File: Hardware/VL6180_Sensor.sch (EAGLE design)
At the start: 23 parts, among them U1 VL6180, U3 MIC5219 3.3V

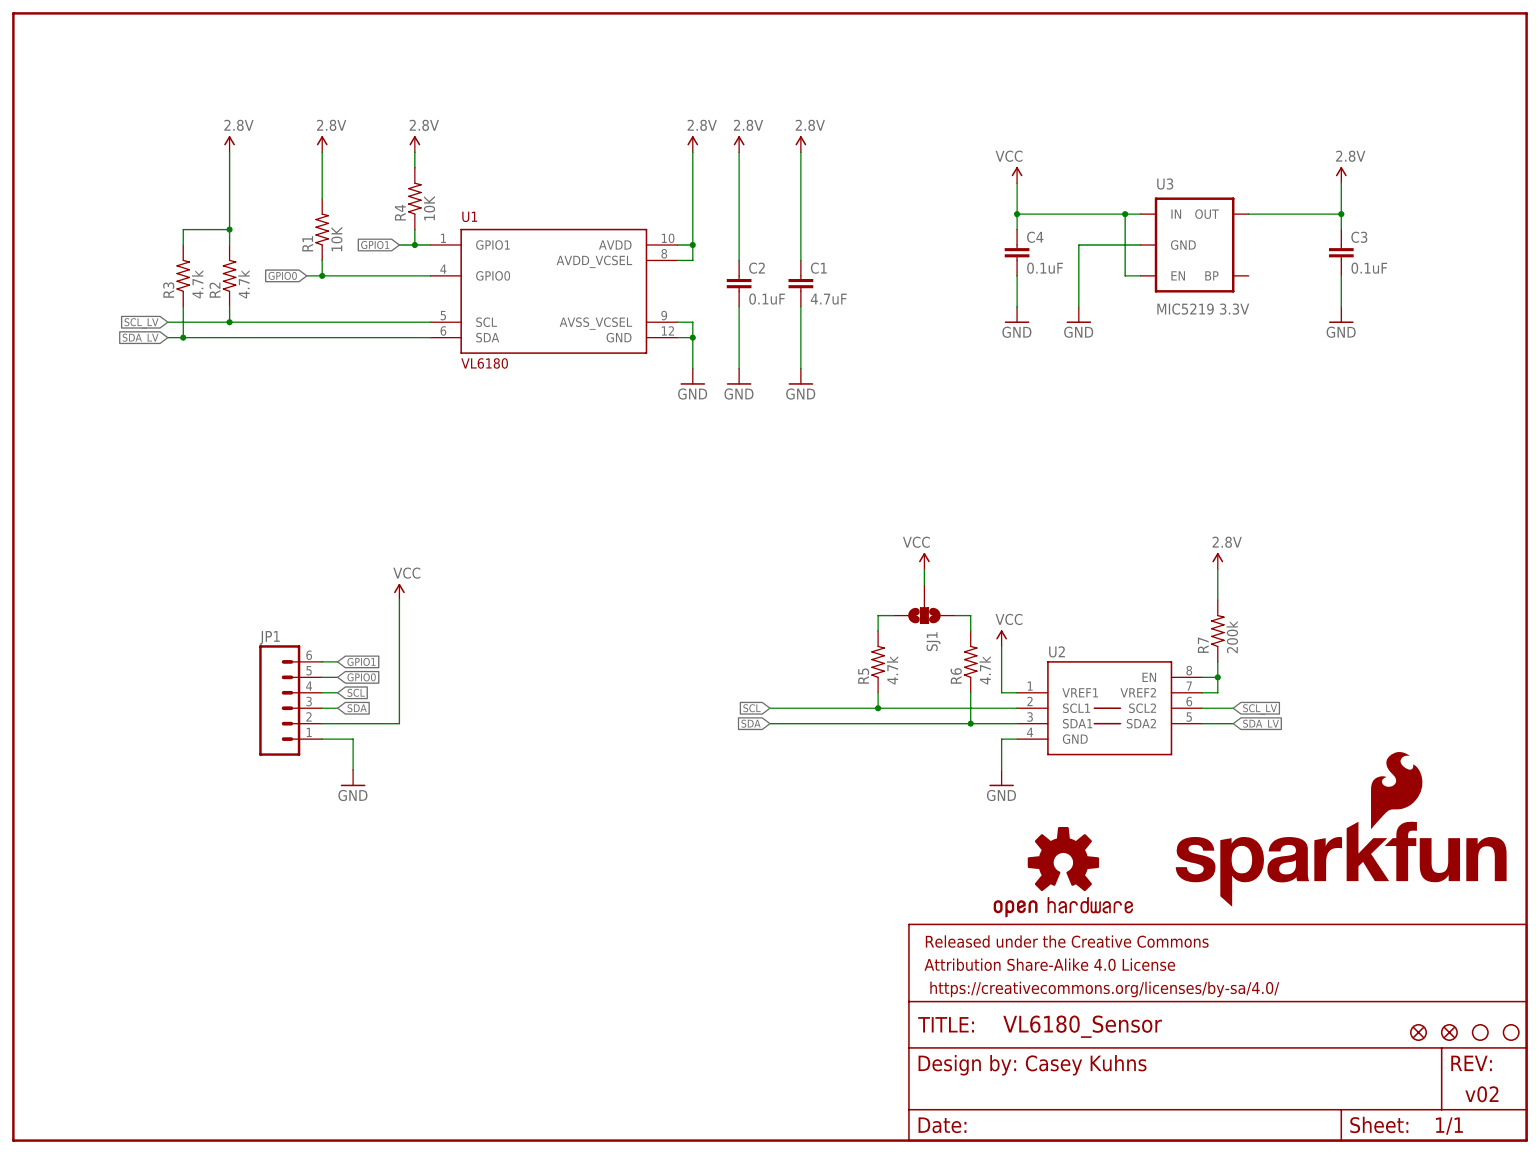
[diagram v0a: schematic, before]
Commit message: modified:   Hardware/VL6180_Breakout.brd 	modified:   Hardware/VL6180_Breakout.sch 	renamed:    Hardware/VL6180.brd -> Hardware/VL6180_Sensor.brd 	renamed:    Hardware/VL6180.sch -> Hardware/VL6180_Sensor.sch
Removed I2C level shifter and switched to Fet bases solution.
New solderpaste footprint for VL6180 for improved reflow.
updated all parts with Sparkle ID's
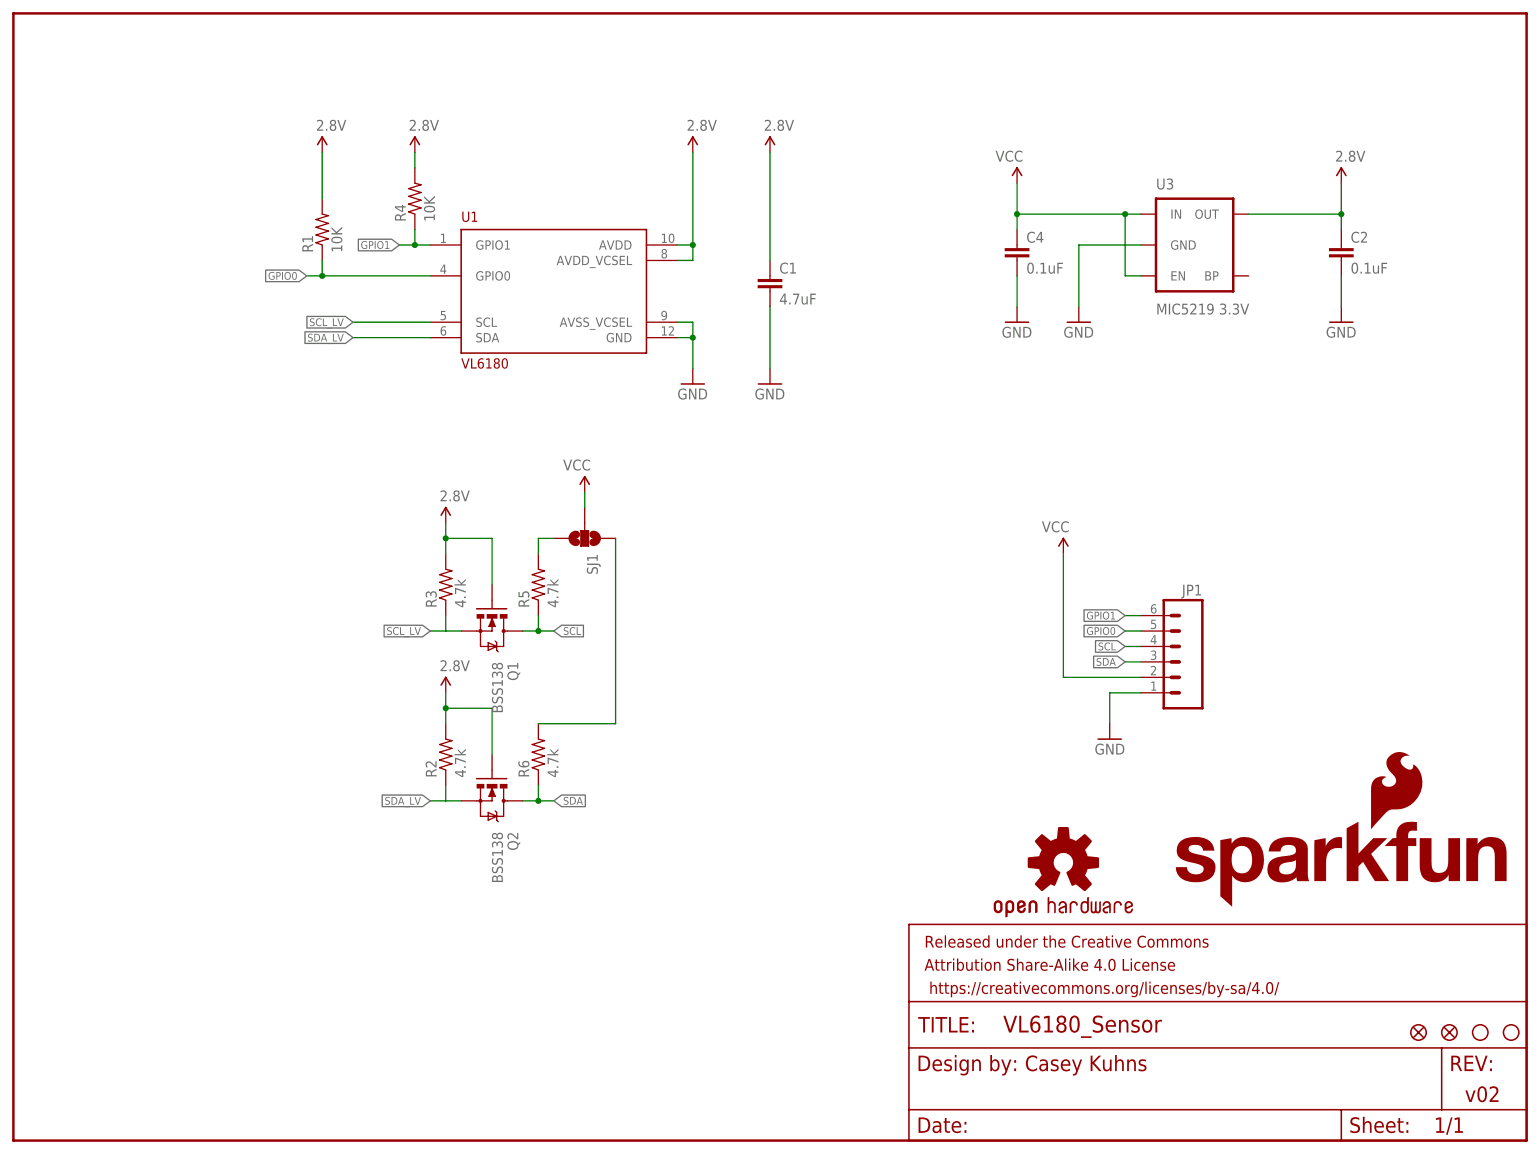
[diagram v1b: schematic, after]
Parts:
- removed C3: 0.1uF, SparkFun-Capacitors:0.1UF-25V(+80/-20%)(0603)
- removed R7: 200k, SparkFun-Resistors:200KOHM1/10W1%(0603)200K
- removed U2: (no value), SparkFun-DigitalIC:PCA9306
- added Q1, Q2: BSS138, SparkFun-DiscreteSemi:MOSFET-NCHANNELBSS138
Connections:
- removed net N$1: R7.1, U2.EN, U2.VREF2
- net 2.8V: now also Q1.G, Q2.G; no longer C3.1, R7.2
- net GND: no longer C3.2, U2.GND
- net SCL: now also Q1.D; no longer U2.SCL1
- net SCL_LV: now also Q1.S, R3.1; no longer R2.1, U2.SCL2
- net SDA: now also Q2.D; no longer U2.SDA1
- net SDA_LV: now also Q2.S, R2.1; no longer R3.1, U2.SDA2
- net VCC: no longer U2.VREF1
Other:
- moved on the sheet: C1, C2, JP1, R2, R3, R5, R6, SJ1

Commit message: changed I2C resistors to 2.2k, added current limiting resistor on GPIO pins.
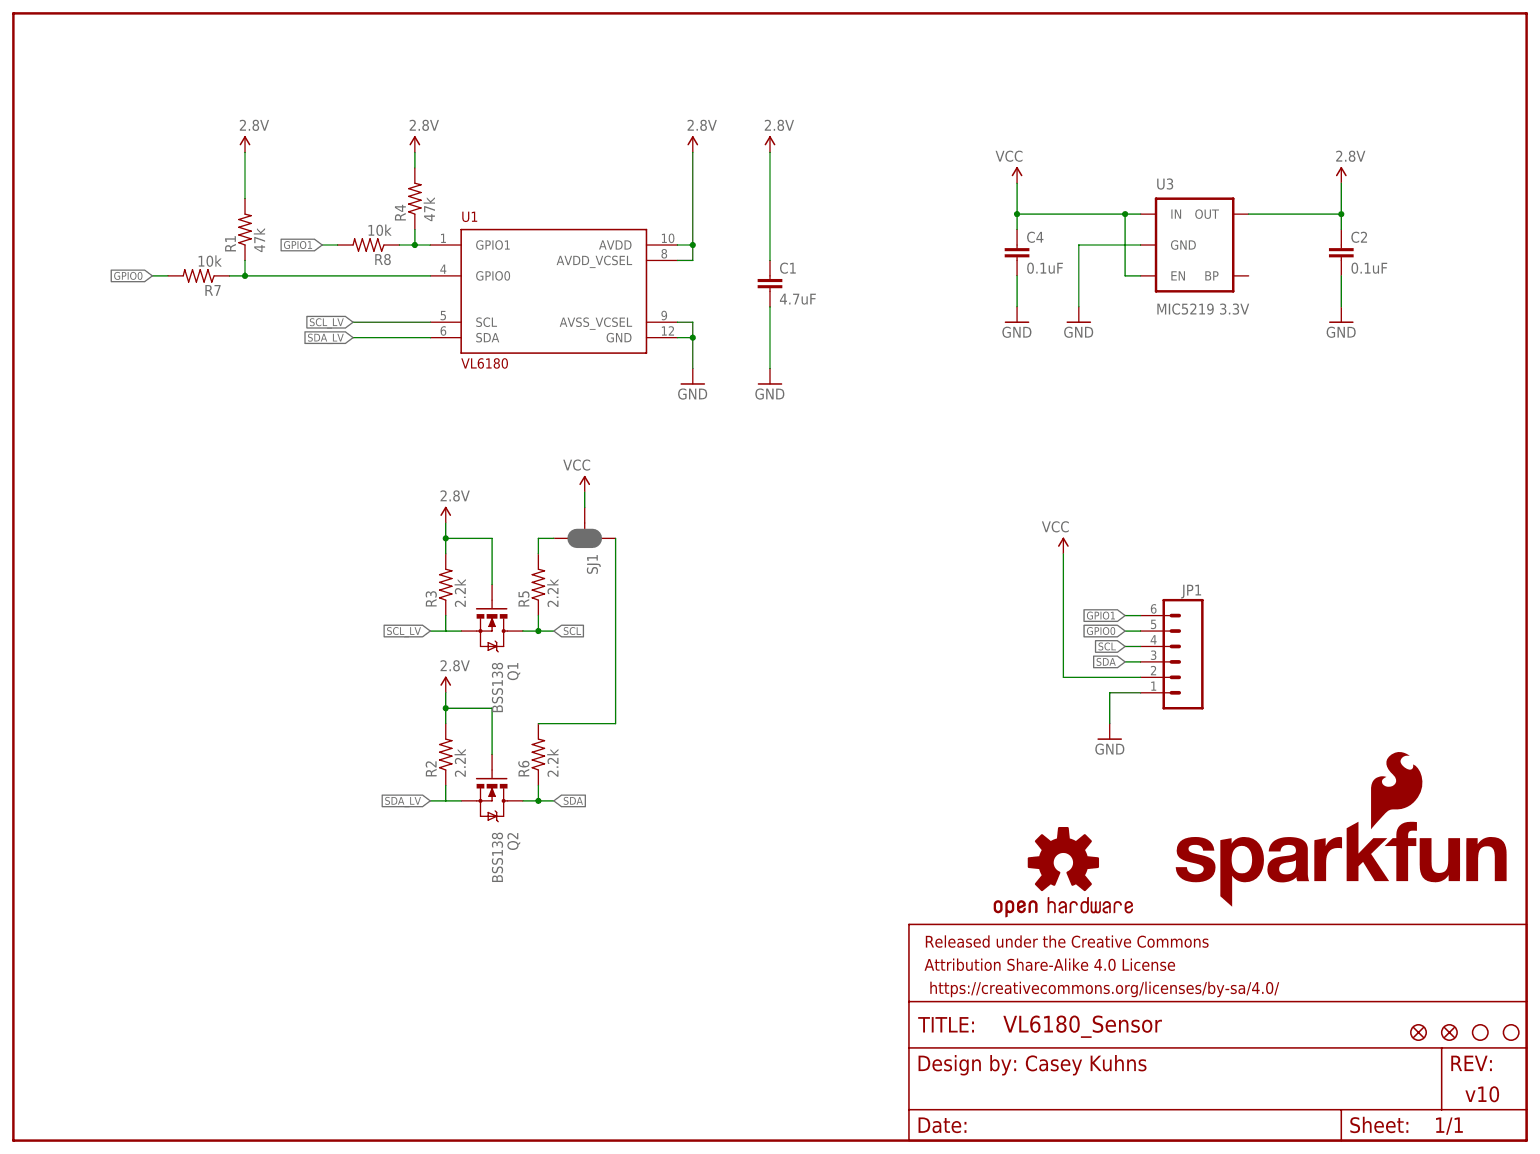
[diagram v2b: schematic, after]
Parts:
- added R7, R8: 10k, SparkFun-Resistors:10KOHM1/10W1%(0603)0603
- R1, R4: value 10K -> 47k; device SparkFun-Resistors:10KOHM1/10W1%(0603)0603 -> SparkFun-Resistors:47KOHM1/10W1%(0603)
- R2, R3, R5, R6: value 4.7k -> 2.2k; device SparkFun-Resistors:4.7KOHM1/10W1%(0603) -> SparkFun-Resistors:2.2KOHM1/10W1%(0603)
- SJ1: value (none) -> JUMPER-PAD-3-NC_BY_PASTE; device SparkFun-Passives:SOLDERJUMPER_2WAYPASTE1&2&3 -> SparkFun-Passives:JUMPER-PAD-3-NC_BY_PASTE
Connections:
- new net N$100: R1.1, R7.1, U1.GPIO0
- new net N$103: R4.1, R8.1, U1.GPIO1
- net GPIO0: now also R7.2; no longer R1.1, U1.GPIO0
- net GPIO1: now also R8.2; no longer R4.1, U1.GPIO1
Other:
- note added: "v10"
- note removed: "v02"
- moved on the sheet: R1
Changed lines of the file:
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@@
 <part name="FRAME1" library="SparkFun-Aesthetics" deviceset="FRAME-LETTER" device=""/>
 <part name="U1" library="VL6180" deviceset="VL6180" device=""/>
-<part name="SJ1" library="SparkFun-Passives" deviceset="SOLDERJUMPER_2WAY" device="PASTE1&amp;2&amp;3"/>
-<part name="R2" library="SparkFun-Resistors" deviceset="4.7KOHM1/10W1%(0603)" device="" value="4.7k"/>
-<part name="R3" library="SparkFun-Resistors" deviceset="4.7KOHM1/10W1%(0603)" device="" value="4.7k"/>
-<part name="R4" library="SparkFun-Resistors" deviceset="10KOHM1/10W1%(0603)" device="0603" value="10K"/>
+<part name="SJ1" library="SparkFun-Passives" deviceset="JUMPER-PAD-3-NC_BY_PASTE" device="" value=""/>
+<part name="R2" library="SparkFun-Resistors" deviceset="2.2KOHM1/10W1%(0603)" device="" value="2.2k"/>
+<part name="R3" library="SparkFun-Resistors" deviceset="2.2KOHM1/10W1%(0603)" device="" value="2.2k"/>
+<part name="R4" library="SparkFun-Resistors" deviceset="47KOHM1/10W1%(0603)" device="" value="47k"/>
 <part name="C1" library="SparkFun-Capacitors" deviceset="4.7UF-6.3V-10%(0603)" device="0603" value="4.7uF"/>
 <part name="C2" library="SparkFun-Capacitors" deviceset="0.1UF-25V(+80/-20%)(0603)" device="" value="0.1uF"/>
@@
 <part name="SUPPLY8" library="SparkFun-Aesthetics" deviceset="2.8V" device=""/>
 <part name="SUPPLY9" library="SparkFun-Aesthetics" deviceset="2.8V" device=""/>
-<part name="R5" library="SparkFun-Resistors" deviceset="4.7KOHM1/10W1%(0603)" device="" value="4.7k"/>
-<part name="R6" library="SparkFun-Resistors" deviceset="4.7KOHM1/10W1%(0603)" device="" value="4.7k"/>
+<part name="R5" library="SparkFun-Resistors" deviceset="2.2KOHM1/10W1%(0603)" device="" value="2.2k"/>
+<part name="R6" library="SparkFun-Resistors" deviceset="2.2KOHM1/10W1%(0603)" device="" value="2.2k"/>
 <part name="SUPPLY10" library="SparkFun-Aesthetics" deviceset="VCC" device=""/>
 <part name="GND6" library="SparkFun-Aesthetics" deviceset="GND" device=""/>
@@
 <part name="GND8" library="SparkFun-Aesthetics" deviceset="GND" device=""/>
 <part name="SUPPLY12" library="SparkFun-Aesthetics" deviceset="VCC" device=""/>
-<part name="R1" library="SparkFun-Resistors" deviceset="10KOHM1/10W1%(0603)" device="0603" value="10K"/>
+<part name="R1" library="SparkFun-Resistors" deviceset="47KOHM1/10W1%(0603)" device="" value="47k"/>
 <part name="LOGO1" library="SparkFun-Aesthetics" deviceset="SFE_LOGO_NAME_FLAME" device=".1_INCH"/>
 <part name="LOGO2" library="SparkFun-Aesthetics" deviceset="OSHW-LOGO" device="S"/>
@@
 <part name="Q2" library="SparkFun-DiscreteSemi" deviceset="MOSFET-NCHANNEL" device="BSS138" value="BSS138"/>
 <part name="SUPPLY4" library="SparkFun-Aesthetics" deviceset="2.8V" device=""/>
+<part name="R7" library="SparkFun-Resistors" deviceset="10KOHM1/10W1%(0603)" device="0603" value="10k"/>
+<part name="R8" library="SparkFun-Resistors" deviceset="10KOHM1/10W1%(0603)" device="0603" value="10k"/>
 </parts>
 <sheets>
@@
 <plain>
 <text x="166.37" y="11.43" size="2.54" layer="94">Casey Kuhns</text>
-<text x="238.76" y="6.35" size="2.54" layer="94">v02</text>
+<text x="238.76" y="6.35" size="2.54" layer="94">v10</text>
 </plain>
 <instances>
@@
 <instance part="SUPPLY6" gate="G$1" x="172.72" y="96.52" rot="MR0"/>
 <instance part="SUPPLY7" gate="G$1" x="66.04" y="162.56"/>
-<instance part="SUPPLY8" gate="G$1" x="50.8" y="162.56"/>
+<instance part="SUPPLY8" gate="G$1" x="38.1" y="162.56"/>
 <instance part="SUPPLY9" gate="G$1" x="71.12" y="101.6"/>
 <instance part="R5" gate="G$1" x="86.36" y="91.44" rot="R90"/>
@@
 <instance part="GND8" gate="1" x="175.26" y="134.62"/>
 <instance part="SUPPLY12" gate="G$1" x="93.98" y="106.68" rot="MR0"/>
-<instance part="R1" gate="G$1" x="50.8" y="149.86" rot="R90"/>
+<instance part="R1" gate="G$1" x="38.1" y="149.86" rot="R90"/>
 <instance part="LOGO1" gate="G$1" x="190.5" y="38.1"/>
 <instance part="LOGO2" gate="G$1" x="172.72" y="45.72"/>
@@
 </instance>
 <instance part="SUPPLY4" gate="G$1" x="71.12" y="73.66"/>
+<instance part="R7" gate="G$1" x="30.48" y="142.24" rot="R180"/>
+<instance part="R8" gate="G$1" x="58.42" y="147.32" rot="R180"/>
 </instances>
 <busses>
@@
 <net name="GPIO0" class="0">
 <segment>
-<pinref part="U1" gate="G$1" pin="GPIO0"/>
-<wire x1="68.58" y1="142.24" x2="50.8" y2="142.24" width="0.1524" layer="91"/>
-<wire x1="50.8" y1="142.24" x2="50.8" y2="144.78" width="0.1524" layer="91"/>
-<wire x1="50.8" y1="142.24" x2="48.26" y2="142.24" width="0.1524" layer="91"/>
-<label x="48.26" y="142.24" size="1.27" layer="95" rot="R180" xref="yes"/>
-<junction x="50.8" y="142.24"/>
-<pinref part="R1" gate="G$1" pin="1"/>
-</segment>
-<segment>
 <pinref part="JP1" gate="G$1" pin="5"/>
 <wire x1="185.42" y1="83.82" x2="182.88" y2="83.82" width="0.1524" layer="91"/>
 <label x="182.88" y="83.82" size="1.27" layer="95" rot="MR0" xref="yes"/>
+</segment>
+<segment>
+<pinref part="R7" gate="G$1" pin="2"/>
+<wire x1="25.4" y1="142.24" x2="22.86" y2="142.24" width="0.1524" layer="91"/>
+<label x="22.86" y="142.24" size="1.27" layer="95" rot="R180" xref="yes"/>
 </segment>
 </net>
@@
 <net name="GPIO1" class="0">
 <segment>
-<pinref part="U1" gate="G$1" pin="GPIO1"/>
-<wire x1="68.58" y1="147.32" x2="66.04" y2="147.32" width="0.1524" layer="91"/>
-<pinref part="R4" gate="G$1" pin="1"/>
-<wire x1="66.04" y1="147.32" x2="66.04" y2="149.86" width="0.1524" layer="91"/>
-<wire x1="66.04" y1="147.32" x2="63.5" y2="147.32" width="0.1524" layer="91"/>
-<label x="63.5" y="147.32" size="1.27" layer="95" rot="R180" xref="yes"/>
-<junction x="66.04" y="147.32"/>
-</segment>
-<segment>
 <pinref part="JP1" gate="G$1" pin="6"/>
 <wire x1="185.42" y1="86.36" x2="182.88" y2="86.36" width="0.1524" layer="91"/>
 <label x="182.88" y="86.36" size="1.27" layer="95" rot="MR0" xref="yes"/>
+</segment>
+<segment>
+<pinref part="R8" gate="G$1" pin="2"/>
+<wire x1="53.34" y1="147.32" x2="50.8" y2="147.32" width="0.1524" layer="91"/>
+<label x="50.8" y="147.32" size="1.27" layer="95" rot="R180" xref="yes"/>
 </segment>
 </net>
@@
 </segment>
 <segment>
-<wire x1="50.8" y1="154.94" x2="50.8" y2="162.56" width="0.1524" layer="91"/>
+<wire x1="38.1" y1="154.94" x2="38.1" y2="162.56" width="0.1524" layer="91"/>
 <pinref part="SUPPLY8" gate="G$1" pin="2.8V"/>
 <pinref part="R1" gate="G$1" pin="2"/>
@@
 </segment>
 </net>
+<net name="N$100" class="0">
+<segment>
+<pinref part="U1" gate="G$1" pin="GPIO0"/>
+<wire x1="68.58" y1="142.24" x2="38.1" y2="142.24" width="0.1524" layer="91"/>
+<wire x1="38.1" y1="142.24" x2="38.1" y2="144.78" width="0.1524" layer="91"/>
+<junction x="38.1" y="142.24"/>
+<pinref part="R1" gate="G$1" pin="1"/>
+<wire x1="35.56" y1="142.24" x2="38.1" y2="142.24" width="0.1524" layer="91"/>
+<pinref part="R7" gate="G$1" pin="1"/>
+</segment>
+</net>
+<net name="N$103" class="0">
+<segment>
+<pinref part="U1" gate="G$1" pin="GPIO1"/>
+<wire x1="68.58" y1="147.32" x2="66.04" y2="147.32" width="0.1524" layer="91"/>
+<pinref part="R4" gate="G$1" pin="1"/>
+<wire x1="66.04" y1="147.32" x2="66.04" y2="149.86" width="0.1524" layer="91"/>
+<wire x1="66.04" y1="147.32" x2="63.5" y2="147.32" width="0.1524" layer="91"/>
+<junction x="66.04" y="147.32"/>
+<pinref part="R8" gate="G$1" pin="1"/>
+</segment>
+</net>
